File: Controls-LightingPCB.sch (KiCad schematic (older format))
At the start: 14 parts, among them J1 MinionConn, U1 LTC6820, U2 HX1188FNL

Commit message: Changed Schematic, but not PCB layout. Updated LED resistor values
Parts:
- added U3: MCP23S17_SO, Package_SO:SOIC-28W_7.5x17.9mm_P1.27mm, symbol Interface_Expansion:MCP23S17_SO
- J1: symbol Connector_Generic:Conn_01x04 -> Connector_Generic:Conn_01x05
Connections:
- net labels added: A_CNCTR, BPS_FAULT, BPS_PWR, CRUZ_EN, CRUZ_ST, CS, CTRL_FAULT, FOR_SW, HZD_SW, Headlight_ON, Headlight_SW, LEFT_BLINK, LEFT_SW, MISO, MOSI, M_CNCTR, REGEN_SW, REV_SW, RIGHT_BLINK, RIGHT_SW, SCK
- wire segments 79 -> 94
- no-connect marks 8 -> 10
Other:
- moved on the sheet: C1, C2, H1, H2, H3, H4, R1, R11, R12, U1, U2

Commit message: Reformatted PCB layout with schematic changes
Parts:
- J1: footprint Connector_Molex:Molex_Micro-Fit_3.0_43650-0400_1x04_P3.00mm_Horizontal -> Connector_Molex:Molex_Micro-Fit_3.0_43650-0500_1x05_P3.00mm_Horizontal
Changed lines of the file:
@@
 F 0 "J1" H 9730 4742 50  0000 L CNN
 F 1 "MinionConn" H 9730 4651 50  0000 L CNN
-F 2 "Connector_Molex:Molex_Micro-Fit_3.0_43650-0400_1x04_P3.00mm_Horizontal" H 9650 4750 50  0001 C CNN
+F 2 "Connector_Molex:Molex_Micro-Fit_3.0_43650-0500_1x05_P3.00mm_Horizontal" H 9650 4750 50  0001 C CNN
 F 3 "~" H 9650 4750 50  0001 C CNN
 	1    9650 4750

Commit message: Board finished with the new changes, needs to be checked
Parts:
- J1: footprint Connector_Molex:Molex_Micro-Fit_3.0_43650-0500_1x05_P3.00mm_Horizontal -> Connector_Molex:Molex_Micro-Fit_3.0_43650-0700_1x07_P3.00mm_Horizontal; symbol Connector_Generic:Conn_01x05 -> Connector_Generic:Conn_01x07
- LOGO1: value Logo_Placeholder -> Dr. Hallock Logo
- LOGO2: value Logo_Placeholder -> UTSVT Logo
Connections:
- net labels added: BPS_FAULT+, BPS_FAULT-
- net labels removed: BPS_FAULT
- wire segments 94 -> 97
- no-connect marks 10 -> 11
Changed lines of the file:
@@
 Text Label 5300 3150 2    50   ~ 0
 FOR_SW
-Text Label 5300 2650 2    50   ~ 0
+Text Label 5300 2750 2    50   ~ 0
 HZD_SW
 Text Label 5300 2950 2    50   ~ 0
@@
 Text Label 5300 1950 2    50   ~ 0
 A_CNCTR
-Wire Wire Line
-	4650 2650 5300 2650
 Text Label 5300 2250 2    50   ~ 0
 LEFT_BLINK
 Text Label 5300 2350 2    50   ~ 0
 RIGHT_BLINK
-Text Label 5300 2550 2    50   ~ 0
-BPS_FAULT
 Text Label 5300 2150 2    50   ~ 0
 CTRL_FAULT
@@
 Wire Wire Line
 	4650 2850 5500 2850
-Wire Wire Line
-	5300 2650 5300 2750
-Wire Wire Line
-	5300 2750 5500 2750
 $Sheet
-S 6500 1750 650  900
+S 6500 1750 650  1050
 U 5F7A71E1
 F0 "ControlLEDs" 50
 F1 "ControlLEDs.sch" 50
-F2 "M_CNCTR" O L 6500 2050 50
-F3 "A_CNCTR" O L 6500 1950 50
-F4 "CTRL_FAULT" O L 6500 2150 50
-F5 "RIGHT_BLINK" O L 6500 2350 50
-F6 "Headlight_ON" O L 6500 2450 50
-F7 "BPS_FAULT" O L 6500 2550 50
-F8 "LEFT_BLINK" O L 6500 2250 50
-F9 "BPS_PWR" O R 7150 1850 50
+F2 "M_CNCTR" I L 6500 2050 50
+F3 "A_CNCTR" I L 6500 1950 50
+F4 "CTRL_FAULT" I L 6500 2150 50
+F5 "RIGHT_BLINK" I L 6500 2350 50
+F6 "Headlight_ON" I L 6500 2450 50
+F7 "LEFT_BLINK" I L 6500 2250 50
+F8 "BPS_PWR" I R 7150 1850 50
+F9 "BPS_FAULT-" I R 7150 2700 50
+F10 "BPS_FAULT+" I R 7150 2600 50
 $EndSheet
-Wire Wire Line
-	4650 2550 6500 2550
 Wire Wire Line
 	4650 2450 6500 2450
@@
 CS
 $Comp
-L Connector_Generic:Conn_01x05 J1
+L Connector_Generic:Conn_01x07 J1
 U 1 1 5FCC2338
 P 9650 4750
 F 0 "J1" H 9730 4742 50  0000 L CNN
 F 1 "MinionConn" H 9730 4651 50  0000 L CNN
-F 2 "Connector_Molex:Molex_Micro-Fit_3.0_43650-0500_1x05_P3.00mm_Horizontal" H 9650 4750 50  0001 C CNN
+F 2 "Connector_Molex:Molex_Micro-Fit_3.0_43650-0700_1x07_P3.00mm_Horizontal" H 9650 4750 50  0001 C CNN
 F 3 "~" H 9650 4750 50  0001 C CNN
 	1    9650 4750
 	1    0    0    -1
 $EndComp
-Wire Wire Line
-	9450 4950 9400 4950
-Wire Wire Line
-	9400 4550 9450 4550
-Wire Wire Line
-	9400 4950 9400 5000
-Wire Wire Line
-	9400 4500 9400 4550
 Wire Wire Line
 	5250 5400 5350 5400
@@
 L power:+12V #PWR0104
 U 1 1 5F7E142C
-P 9400 4500
-F 0 "#PWR0104" H 9400 4350 50  0001 C CNN
-F 1 "+12V" H 9415 4673 50  0000 C CNN
-F 2 "" H 9400 4500 50  0001 C CNN
-F 3 "" H 9400 4500 50  0001 C CNN
-	1    9400 4500
+P 9400 4400
+F 0 "#PWR0104" H 9400 4250 50  0001 C CNN
+F 1 "+12V" H 9415 4573 50  0000 C CNN
+F 2 "" H 9400 4400 50  0001 C CNN
+F 3 "" H 9400 4400 50  0001 C CNN
+	1    9400 4400
 	1    0    0    -1
 $EndComp
@@
 L power:GNDPWR #PWR0103
 U 1 1 5F7E16B8
-P 9400 5000
-F 0 "#PWR0103" H 9400 4800 50  0001 C CNN
-F 1 "GNDPWR" H 9404 4846 50  0000 C CNN
-F 2 "" H 9400 4950 50  0001 C CNN
-F 3 "" H 9400 4950 50  0001 C CNN
-	1    9400 5000
+P 9400 5100
+F 0 "#PWR0103" H 9400 4900 50  0001 C CNN
+F 1 "GNDPWR" H 9404 4946 50  0000 C CNN
+F 2 "" H 9400 5050 50  0001 C CNN
+F 3 "" H 9400 5050 50  0001 C CNN
+	1    9400 5100
 	1    0    0    -1
 $EndComp
@@
 	1    0    0    -1
 $EndComp
-Text Label 7350 1850 0    50   ~ 0
+Text Label 7700 1850 2    50   ~ 0
 BPS_PWR
 Wire Wire Line
 	7150 1850 7700 1850
-Text Label 9050 4650 0    50   ~ 0
+Text Label 8950 4950 0    50   ~ 0
 BPS_PWR
 Wire Wire Line
@@
 Wire Wire Line
 	8300 4850 9450 4850
-Wire Wire Line
-	9050 4650 9450 4650
 $Comp
 L Mechanical:MountingHole H4
@@
 P 8700 1900
 F 0 "LOGO2" H 8700 2050 50  0001 C CNN
-F 1 "Logo_Placeholder" H 8840 1900 50  0000 L CNN
+F 1 "UTSVT Logo" H 8840 1900 50  0000 L CNN
 F 2 "UTSVT_Special:UTSVT_Logo_Symbol" H 8700 1975 50  0001 C CNN
 F 3 "" H 8700 1975 50  0001 C CNN
@@
 P 8700 1600
 F 0 "LOGO1" H 8700 1750 50  0001 C CNN
-F 1 "Logo_Placeholder" H 8840 1600 50  0000 L CNN
+F 1 "Dr. Hallock Logo" H 8840 1600 50  0000 L CNN
 F 2 "UTSVT_Special:Hallock_Image_Small" H 8700 1675 50  0001 C CNN
 F 3 "" H 8700 1675 50  0001 C CNN
@@
 	1    0    0    -1
 $EndComp
+Wire Wire Line
+	9450 5050 9400 5050
+Wire Wire Line
+	9400 5050 9400 5100
+Wire Wire Line
+	9400 4400 9400 4450
+Wire Wire Line
+	9400 4450 9450 4450
+Wire Wire Line
+	4650 2550 4900 2550
+Wire Wire Line
+	4900 2550 4900 2750
+Wire Wire Line
+	4900 2750 5500 2750
+NoConn ~ 4650 2650
+Text Label 8950 4550 0    50   ~ 0
+BPS_FAULT+
+Text Label 8950 4650 0    50   ~ 0
+BPS_FAULT-
+Wire Wire Line
+	8950 4550 9450 4550
+Wire Wire Line
+	8950 4950 9450 4950
+Wire Wire Line
+	8950 4650 9450 4650
+Text Label 7700 2700 2    50   ~ 0
+BPS_FAULT-
+Text Label 7700 2600 2    50   ~ 0
+BPS_FAULT+
+Wire Wire Line
+	7150 2600 7700 2600
+Wire Wire Line
+	7150 2700 7700 2700
 $EndSCHEMATC

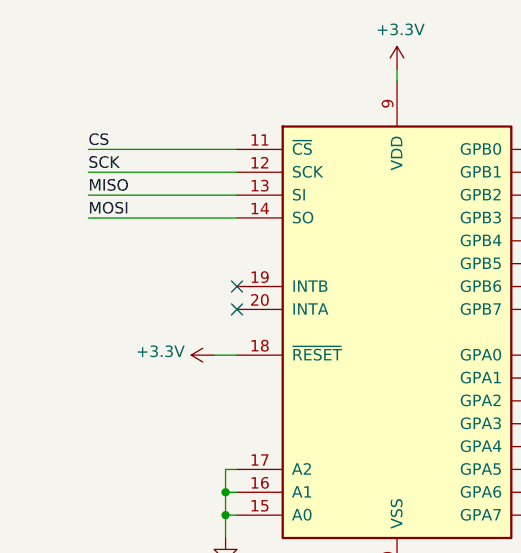
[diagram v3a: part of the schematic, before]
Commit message: Fixes switch/button circuitry
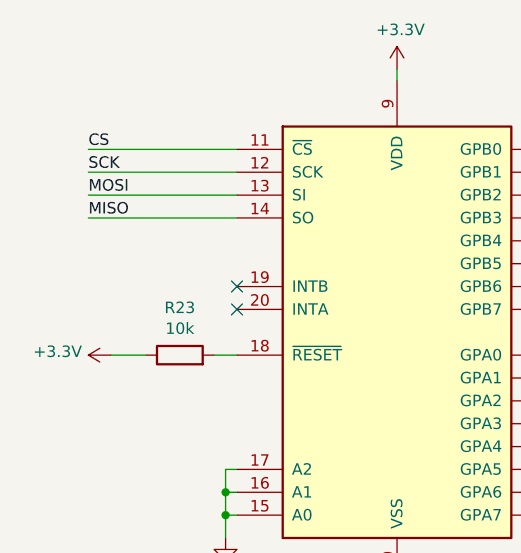
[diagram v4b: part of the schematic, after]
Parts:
- added R23: 10k, Resistor_SMD:R_0805_2012Metric, symbol Device:R
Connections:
- net +3V3: now also R23.1; no longer U3.18 (~RESET~)
- net MISO: now also U3.14 (SO); no longer U3.13 (SI)
- net MOSI: now also U3.13 (SI); no longer U3.14 (SO)
- new net: R23.2, U3.18 (~RESET~)
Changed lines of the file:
@@
 Text Label 2600 2050 0    50   ~ 0
 SCK
+Text Label 2600 2250 0    50   ~ 0
+MISO
 Text Label 2600 2150 0    50   ~ 0
-MISO
-Text Label 2600 2250 0    50   ~ 0
 MOSI
 Wire Wire Line
@@
 L power:+3.3V #PWR?
 U 1 1 5FDEB7F2
-P 3150 2850
+P 2700 2850
 AR Path="/5F78B6DA/5FDEB7F2" Ref="#PWR?"  Part="1"
 AR Path="/5FDEB7F2" Ref="#PWR016"  Part="1"
-F 0 "#PWR016" H 3150 2700 50  0001 C CNN
-F 1 "+3.3V" V 3165 2978 50  0000 L CNN
-F 2 "" H 3150 2850 50  0001 C CNN
-F 3 "" H 3150 2850 50  0001 C CNN
-	1    3150 2850
+F 0 "#PWR016" H 2700 2700 50  0001 C CNN
+F 1 "+3.3V" V 2715 2978 50  0000 L CNN
+F 2 "" H 2700 2850 50  0001 C CNN
+F 3 "" H 2700 2850 50  0001 C CNN
+	1    2700 2850
 	0    -1   -1   0
 $EndComp
@@
 Wire Wire Line
 	7150 2700 7700 2700
+$Comp
+L Device:R R23
+U 1 1 5FE56EF0
+P 3000 2850
+F 0 "R23" V 3207 2850 50  0000 C CNN
+F 1 "10k" V 3116 2850 50  0000 C CNN
+F 2 "Resistor_SMD:R_0805_2012Metric" V 2930 2850 50  0001 C CNN
+F 3 "~" H 3000 2850 50  0001 C CNN
+	1    3000 2850
+	0    -1   -1   0
+$EndComp
+Wire Wire Line
+	2850 2850 2700 2850
 $EndSCHEMATC

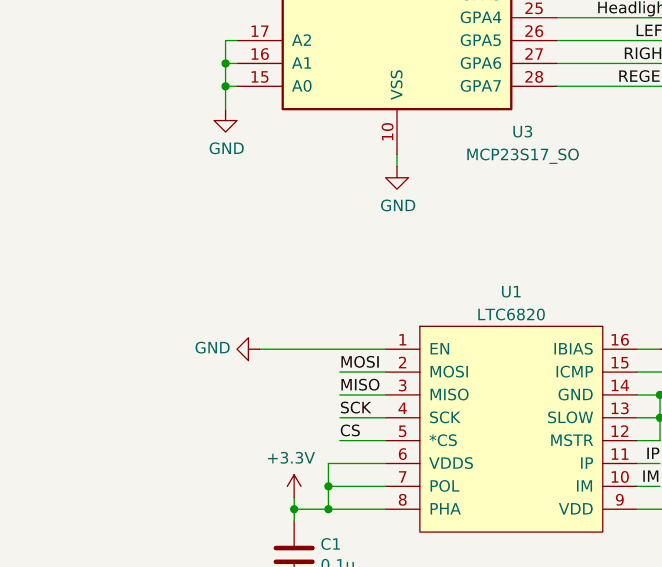
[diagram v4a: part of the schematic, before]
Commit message: Added resistor and diode
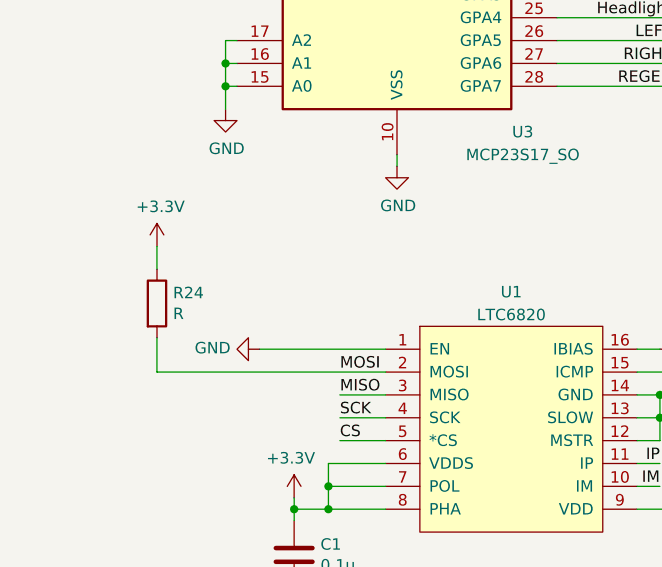
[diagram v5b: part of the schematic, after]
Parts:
- added R24: R, Resistor_SMD:R_0805_2012Metric, symbol Device:R
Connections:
- net +3V3: now also R24.1
- net MOSI: now also R24.2
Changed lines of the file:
@@
 	3700 4900 3900 4900
-Wire Wire Line
-	3700 4800 3900 4800
 Wire Wire Line
 	3900 4700 3350 4700
@@
 Wire Wire Line
 	2850 2850 2700 2850
+$Comp
+L Device:R R24
+U 1 1 61595B5D
+P 2900 4500
+F 0 "R24" H 2970 4546 50  0000 L CNN
+F 1 "R" H 2970 4455 50  0000 L CNN
+F 2 "Resistor_SMD:R_0805_2012Metric" V 2830 4500 50  0001 C CNN
+F 3 "~" H 2900 4500 50  0001 C CNN
+	1    2900 4500
+	1    0    0    -1
+$EndComp
+Wire Wire Line
+	2900 4800 2900 4650
+Wire Wire Line
+	2900 4800 3900 4800
+$Comp
+L power:+3.3V #PWR028
+U 1 1 61599473
+P 2900 4250
+F 0 "#PWR028" H 2900 4100 50  0001 C CNN
+F 1 "+3.3V" H 2915 4423 50  0000 C CNN
+F 2 "" H 2900 4250 50  0001 C CNN
+F 3 "" H 2900 4250 50  0001 C CNN
+	1    2900 4250
+	1    0    0    -1
+$EndComp
+Wire Wire Line
+	2900 4350 2900 4250
 $EndSCHEMATC

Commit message: Adds the gerbers
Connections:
- net +3V3: now also U1.13 (SLOW)
- net GND: no longer U1.13 (SLOW)
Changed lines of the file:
@@
 	5650 5400 5750 5400
 Wire Wire Line
-	5000 5400 5250 5400
-Connection ~ 5100 4900
-Wire Wire Line
 	5850 4900 5850 5000
-Wire Wire Line
-	5100 4900 5850 4900
-Connection ~ 5100 5000
-Wire Wire Line
-	5100 4900 5100 5000
-Wire Wire Line
-	5000 4900 5100 4900
-Wire Wire Line
-	5100 5000 5000 5000
-Wire Wire Line
-	5100 5100 5100 5000
-Wire Wire Line
-	5000 5100 5100 5100
 $Comp
 L power:GND #PWR0111
@@
 Wire Wire Line
 	2900 4350 2900 4250
+Wire Wire Line
+	5150 5000 5150 5400
+Wire Wire Line
+	5000 5000 5150 5000
+Wire Wire Line
+	5000 5400 5150 5400
+Wire Wire Line
+	5150 5400 5250 5400
+Connection ~ 5150 5400
+Wire Wire Line
+	5000 5100 5100 5100
+Wire Wire Line
+	5100 5100 5100 4900
+Wire Wire Line
+	5000 4900 5100 4900
+Wire Wire Line
+	5100 4900 5850 4900
+Connection ~ 5100 4900
 $EndSCHEMATC

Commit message: Footprint edit
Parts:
- removed U3: MCP23S17_SO, Package_SO:SOIC-28W_7.5x17.9mm_P1.27mm, symbol Interface_Expansion:MCP23S17_SO
- added U3: MCP23S17_SS, Package_SO:SSOP-28_5.3x10.2mm_P0.65mm, symbol Interface_Expansion:MCP23S17_SS
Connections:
- net +3V3: now also U3.9 (VDD)
- net A_CNCTR: now also U3.1 (GPB0)
- net CRUZ_EN: now also U3.22 (GPA1)
- net CRUZ_ST: now also U3.21 (GPA0)
- net CS: now also U3.11 (~CS~)
- net CTRL_FAULT: now also U3.3 (GPB2)
- net FOR_SW: now also U3.24 (GPA3)
- net GND: now also U3.10 (VSS), U3.15 (A0), U3.16 (A1), U3.17 (A2)
- net HZD_SW: now also U3.7 (GPB6)
- net Headlight_ON: now also U3.6 (GPB5)
- net Headlight_SW: now also U3.25 (GPA4)
- net LEFT_BLINK: now also U3.4 (GPB3)
- net LEFT_SW: now also U3.26 (GPA5)
- net MISO: now also U3.14 (SO)
- net MOSI: now also U3.13 (SI)
- net M_CNCTR: now also U3.2 (GPB1)
- net REGEN_SW: now also U3.28 (GPA7)
- net REV_SW: now also U3.23 (GPA2)
- net RIGHT_BLINK: now also U3.5 (GPB4)
- net RIGHT_SW: now also U3.27 (GPA6)
- net SCK: now also U3.12 (SCK)
- net at R23.2: now also U3.18 (~RESET~)
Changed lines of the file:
@@
 Text Label 5000 3050 0    50   ~ 0
 REV_SW
-$Comp
-L Interface_Expansion:MCP23S17_SO U3
-U 1 1 5FDEB79C
-P 3950 2750
-AR Path="/5FDEB79C" Ref="U3"  Part="1"
-AR Path="/5F768F42/5FDEB79C" Ref="U?"  Part="1"
-AR Path="/5F78B6DA/5FDEB79C" Ref="U?"  Part="1"
-F 0 "U3" H 4500 1750 50  0000 C CNN
-F 1 "MCP23S17_SO" H 4500 1650 50  0000 C CNN
-F 2 "Package_SO:SOIC-28W_7.5x17.9mm_P1.27mm" H 4150 1750 50  0001 L CNN
-F 3 "http://ww1.microchip.com/downloads/en/DeviceDoc/20001952C.pdf" H 4150 1650 50  0001 L CNN
-	1    3950 2750
-	1    0    0    -1
-$EndComp
 $Sheet
 S 5500 2700 650  950
@@
 	5100 4900 5850 4900
 Connection ~ 5100 4900
+$Comp
+L Interface_Expansion:MCP23S17_SS U3
+U 1 1 617DED58
+P 3950 2750
+F 0 "U3" H 3950 4031 50  0000 C CNN
+F 1 "MCP23S17_SS" H 3950 3940 50  0000 C CNN
+F 2 "Package_SO:SSOP-28_5.3x10.2mm_P0.65mm" H 4150 1750 50  0001 L CNN
+F 3 "http://ww1.microchip.com/downloads/en/DeviceDoc/20001952C.pdf" H 4150 1650 50  0001 L CNN
+	1    3950 2750
+	1    0    0    -1
+$EndComp
 $EndSCHEMATC

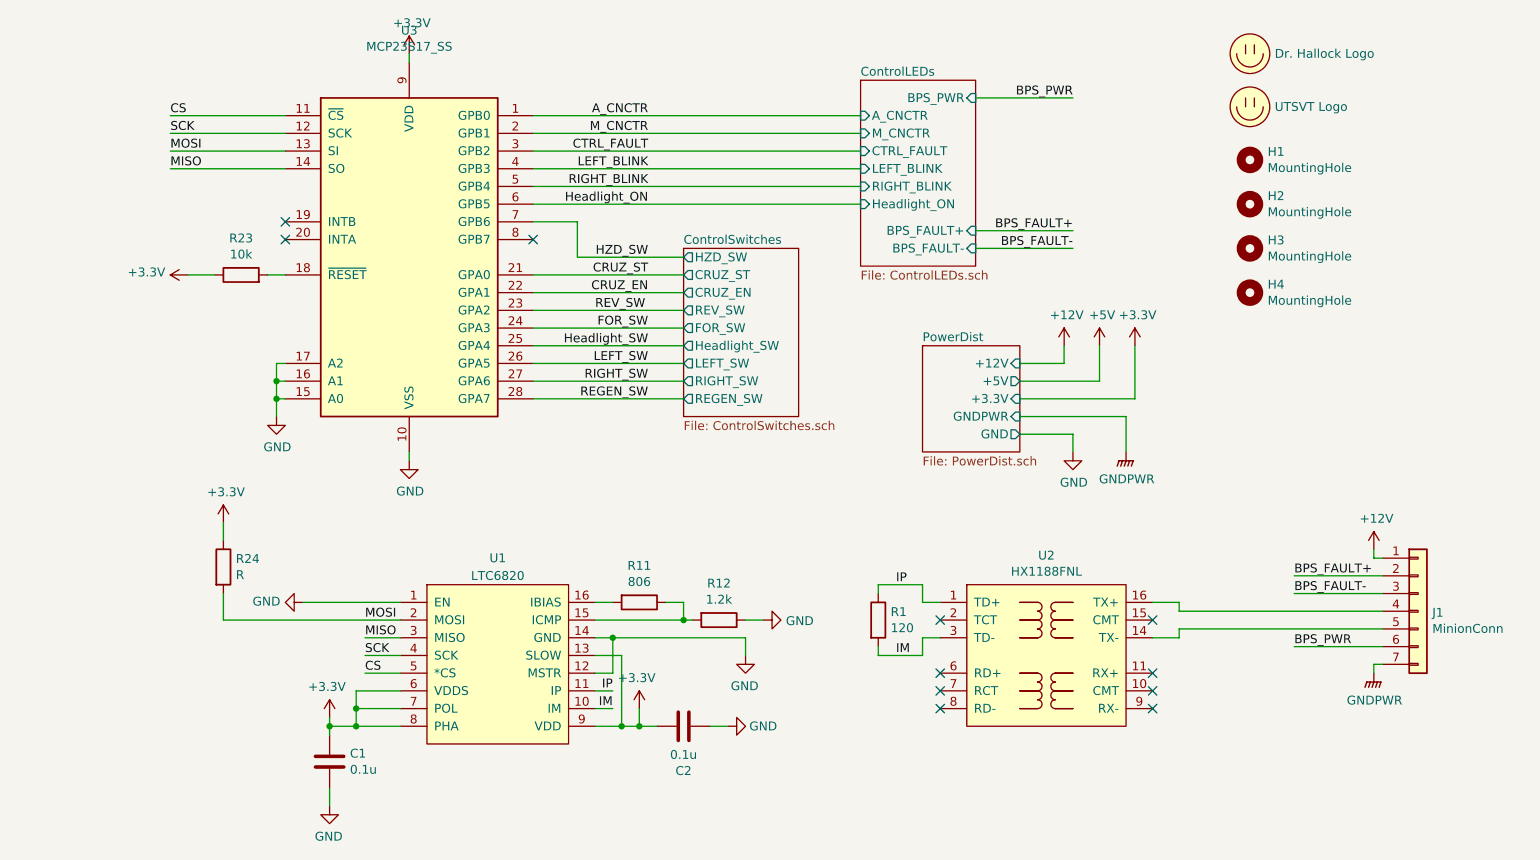
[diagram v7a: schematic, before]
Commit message: isoSPI -> SPI change
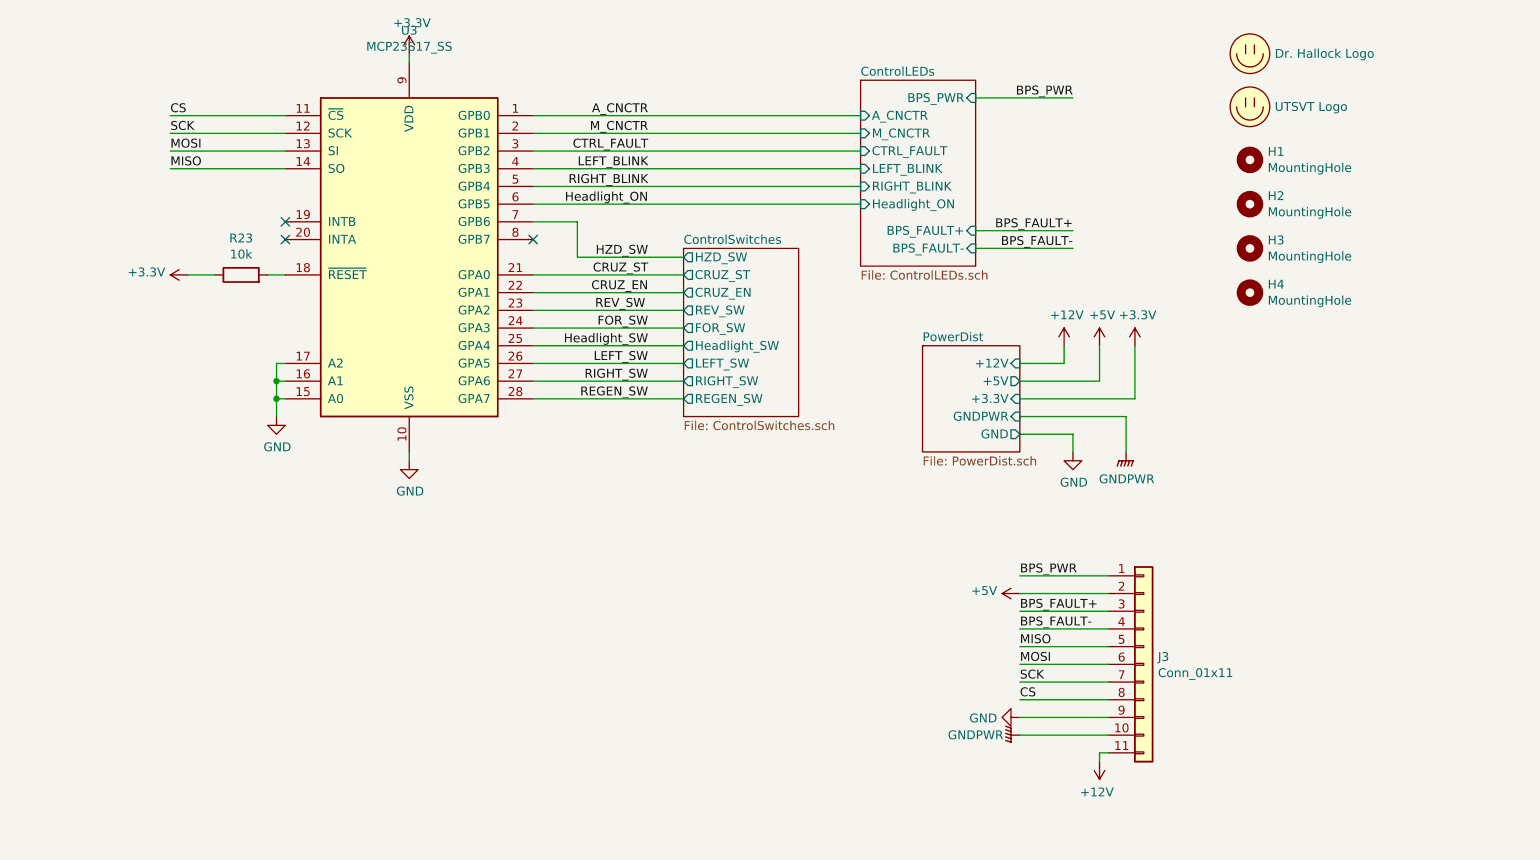
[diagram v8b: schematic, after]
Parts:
- removed C1, C2: 0.1u, Capacitor_SMD:C_0805_2012Metric, symbol Device:C
- removed J1: MinionConn, Connector_Molex:Molex_Micro-Fit_3.0_43650-0700_1x07_P3.00mm_Horizontal, symbol Connector_Generic:Conn_01x07
- removed R1: 120, Resistor_SMD:R_0805_2012Metric, symbol Device:R
- removed R11: 806, Resistor_SMD:R_0805_2012Metric, symbol Device:R
- removed R12: 1.2k, Resistor_SMD:R_0805_2012Metric, symbol Device:R
- removed R24: R, Resistor_SMD:R_0805_2012Metric, symbol Device:R
- removed U1: LTC6820, Package_SO:MSOP-16_3x4mm_P0.5mm, symbol Controls-LightingPCB-rescue:LTC6820-utsvt-chips
- removed U2: HX1188FNL, UTSVT_Passive:HXXXX, symbol Controls-LightingPCB-rescue:HX1188FNL-utsvt-chips
- added J3: Conn_01x11, Connector_Molex:Molex_Micro-Fit_3.0_43650-1100_1x11_P3.00mm_Horizontal, symbol Connector_Generic:Conn_01x11
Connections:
- net +12V: now also J3.11 (Pin_11)
- net +5V: now also J3.2 (Pin_2)
- net BPS_FAULT+: now also J3.3 (Pin_3)
- net BPS_FAULT-: now also J3.4 (Pin_4)
- net BPS_PWR: now also J3.1 (Pin_1)
- net CS: now also J3.8 (Pin_8)
- net GND: now also J3.9 (Pin_9)
- net GNDPWR: now also J3.10 (Pin_10)
- net MISO: now also J3.5 (Pin_5)
- net MOSI: now also J3.6 (Pin_6)
- net SCK: now also J3.7 (Pin_7)
- no-connect marks 11 -> 3
